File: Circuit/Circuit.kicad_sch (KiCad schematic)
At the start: 2 parts, among them Q1 Q_NMOS_DGS, U1 A1302KUA-T

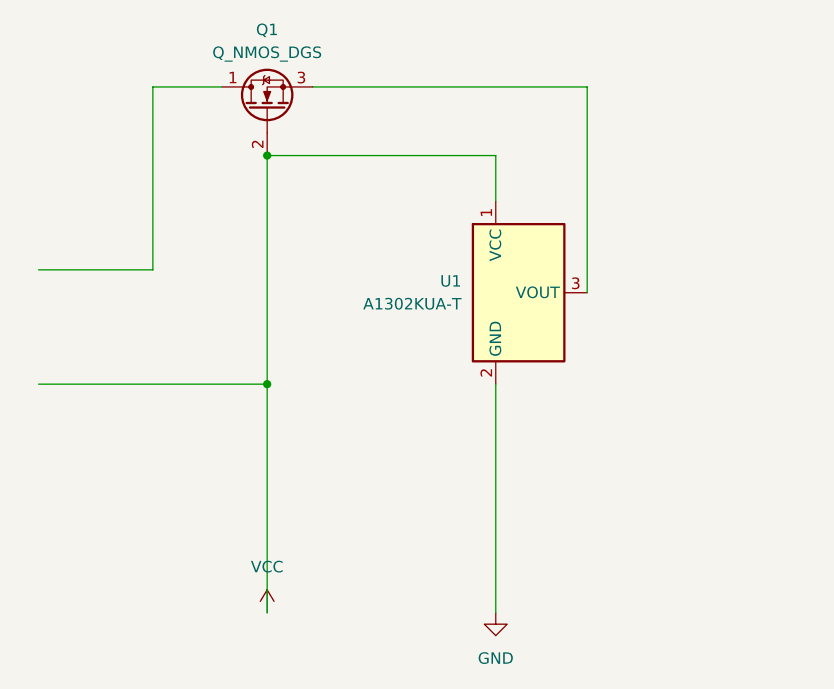
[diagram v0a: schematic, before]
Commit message: Finished circuit, need to test.
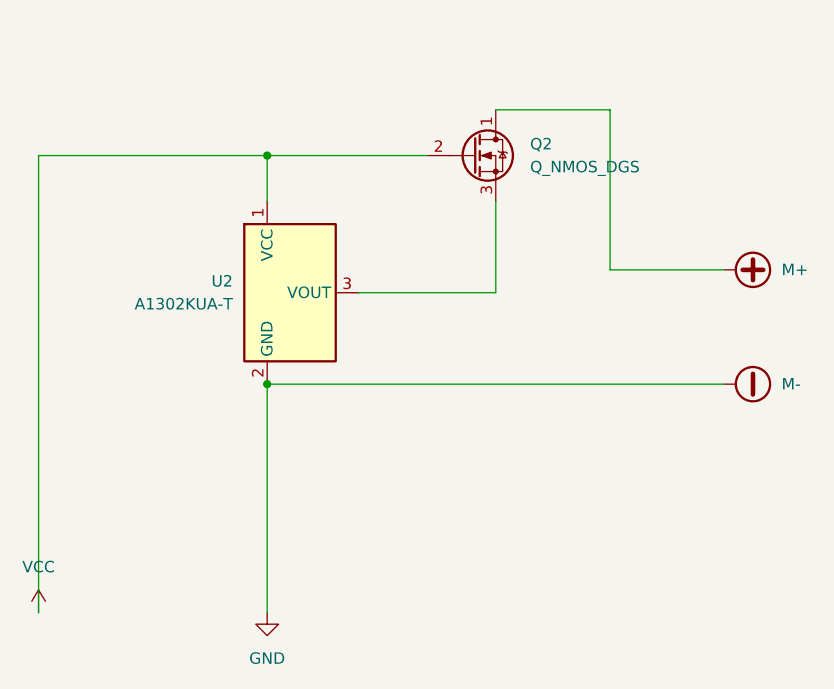
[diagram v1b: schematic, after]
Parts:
- removed Q1: Q_NMOS_DGS, symbol Device:Q_NMOS_DGS
- removed U1: A1302KUA-T, symbol Sensor_Magnetic:A1302KUA-T
- added Q2: Q_NMOS_DGS, symbol Device:Q_NMOS_DGS
- added U2: A1302KUA-T, symbol Sensor_Magnetic:A1302KUA-T
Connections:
- net GND: now also U2.2 (GND)
- net VCC: now also Q2.2 (G), U2.1 (VCC)
- new net: Q2.3 (S), U2.3 (VOUT)
- new net M+: Q2.1 (D)

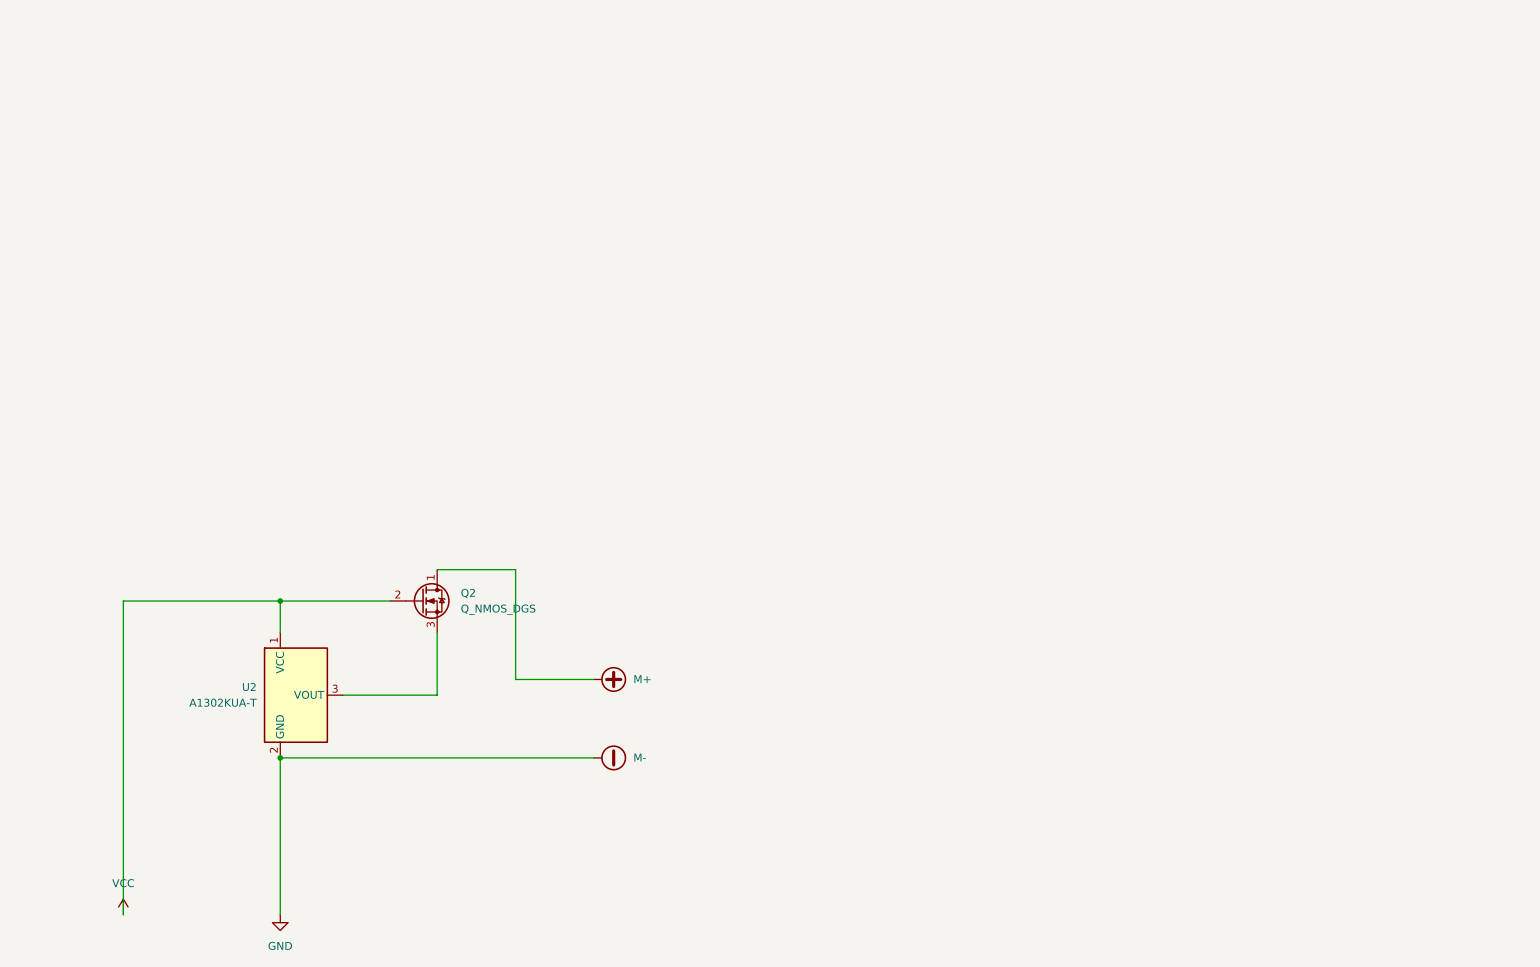
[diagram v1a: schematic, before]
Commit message: Added support for 3 electromagnets and 3 hall chips.
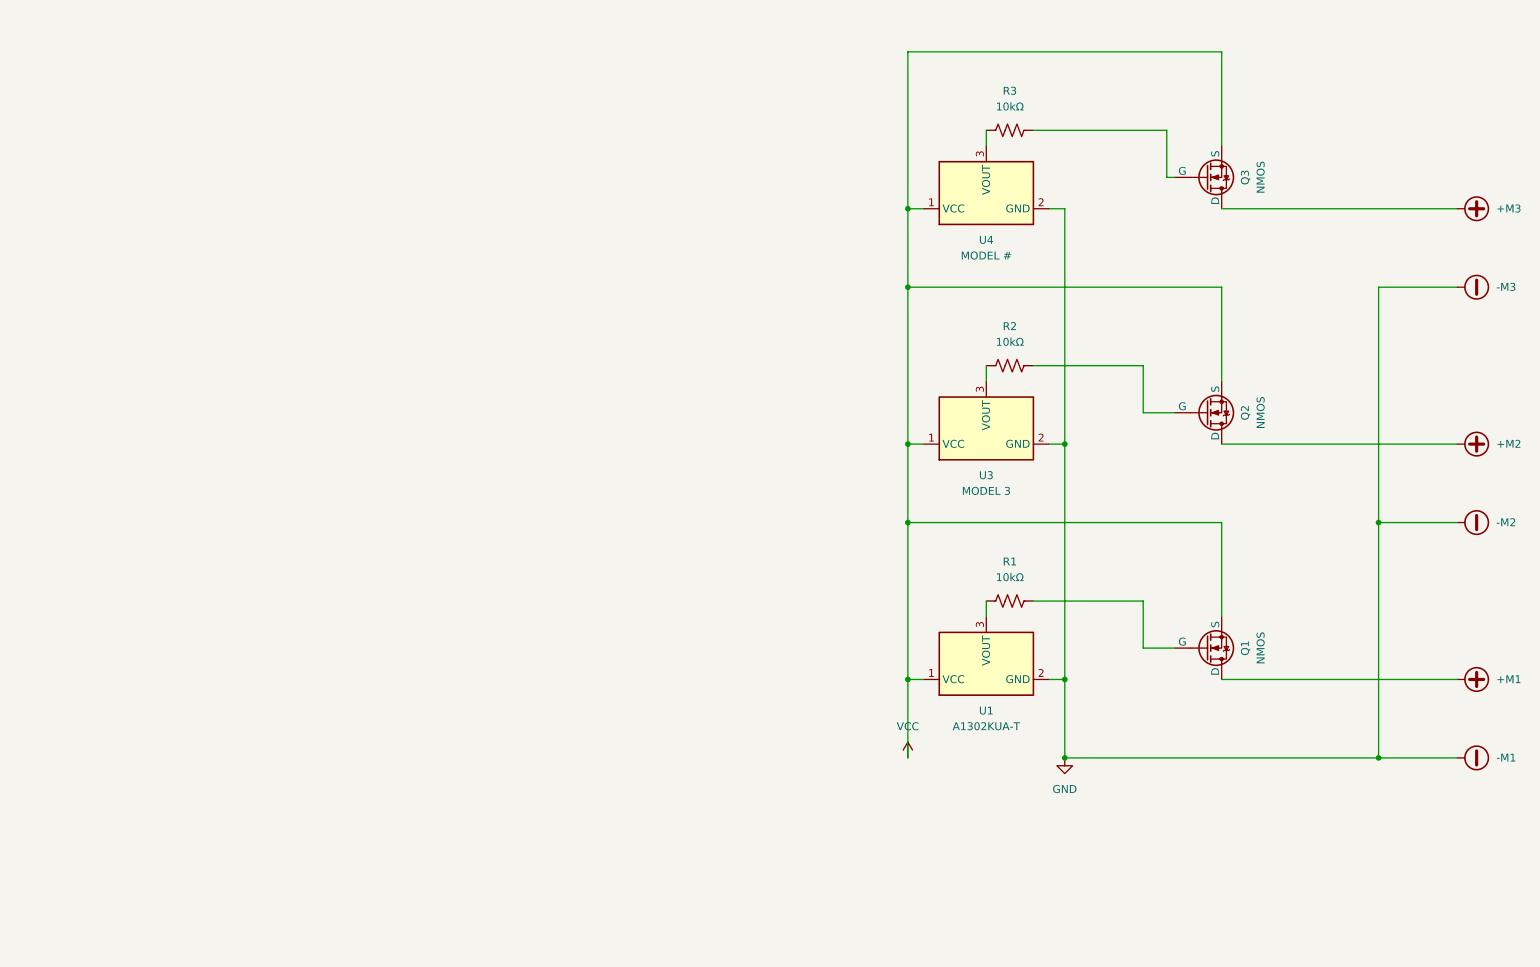
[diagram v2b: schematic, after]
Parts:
- removed Q2: Q_NMOS_DGS, symbol Device:Q_NMOS_DGS
- removed U2: A1302KUA-T, symbol Sensor_Magnetic:A1302KUA-T
- added Q1, Q2, Q3: NMOS, symbol Simulation_SPICE:NMOS
- added R1, R2, R3: 10kΩ, symbol Device:R_US
- added U1: A1302KUA-T, symbol Sensor_Magnetic:A1302KUA-T
- added U3: MODEL 3, symbol Sensor_Magnetic:A1302KUA-T
- added U4: MODEL #, symbol Sensor_Magnetic:A1302KUA-T
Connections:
- net VCC: now also Q1.3 (S), Q2.3 (S), Q3.3 (S), U1.1 (VCC), U3.1 (VCC), U4.1 (VCC)
- new net: Q1.2 (G), R1.2
- new net: R3.1, U4.3 (VOUT)
- new net: Q3.2 (G), R3.2
- new net: Q2.2 (G), R2.2
- new net: R2.1, U3.3 (VOUT)
- new net: R1.1, U1.3 (VOUT)
- new net +M1: Q1.1 (D)
- new net +M2: Q2.1 (D)
- new net +M3: Q3.1 (D)
- new net -M1: U1.2 (GND), U3.2 (GND), U4.2 (GND)

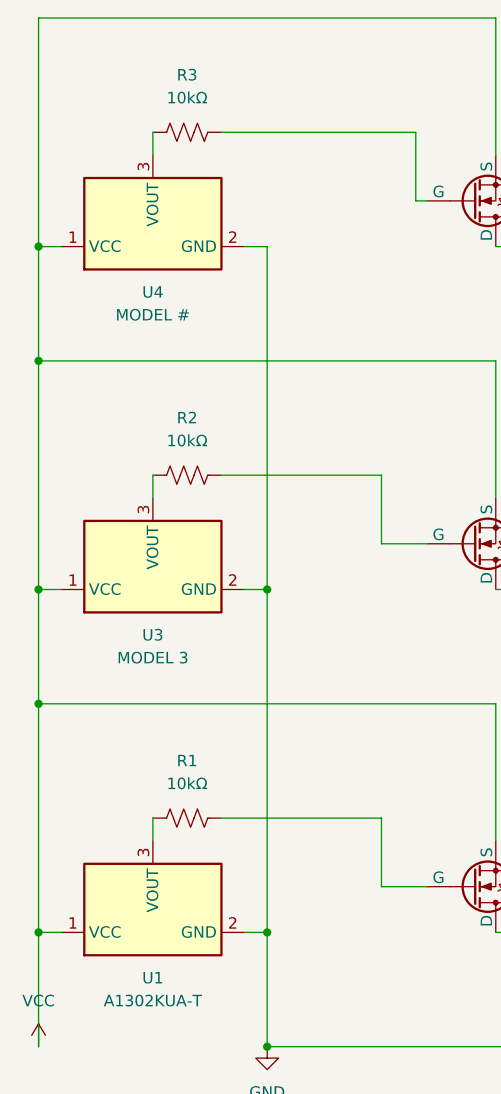
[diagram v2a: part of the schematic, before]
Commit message: Fixed resistors
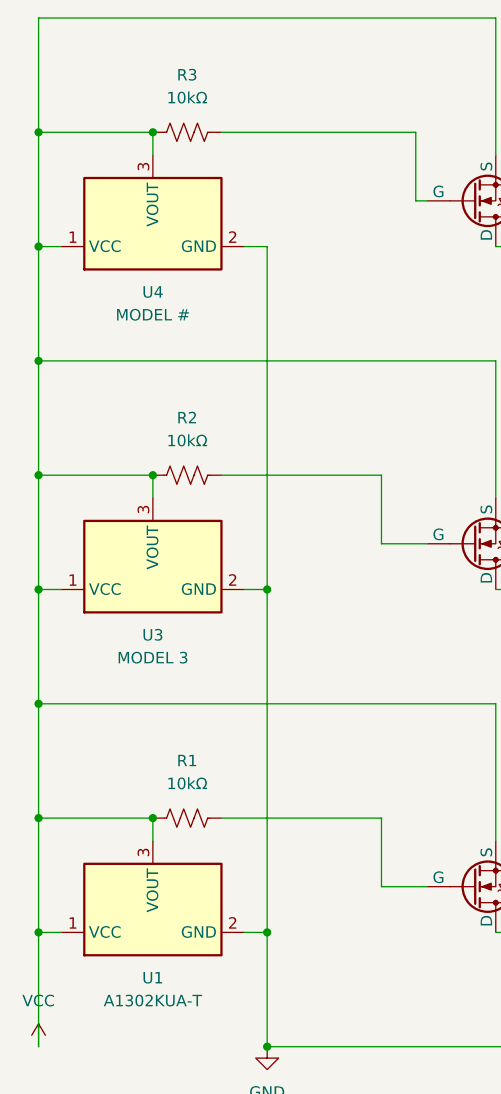
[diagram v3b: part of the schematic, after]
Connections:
- net VCC: now also R1.1, R2.1, R3.1, U1.3 (VOUT), U3.3 (VOUT), U4.3 (VOUT)
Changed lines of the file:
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@@
+	)
+	(junction
+		(at 177.8 139.7)
+		(diameter 0)
+		(color 0 0 0 0)
 	)
 	(junction
@@
 	)
 	(junction
+		(at 165.1 63.5)
+		(diameter 0)
+		(color 0 0 0 0)
+	)
+	(junction
 		(at 241.3 165.1)
 		(diameter 0)
@@
 	)
 	(junction
+		(at 177.8 101.6)
+		(diameter 0)
+		(color 0 0 0 0)
+	)
+	(junction
+		(at 165.1 101.6)
+		(diameter 0)
+		(color 0 0 0 0)
+	)
+	(junction
+		(at 165.1 139.7)
+		(diameter 0)
+		(color 0 0 0 0)
+	)
+	(junction
+		(at 177.8 63.5)
+		(diameter 0)
+		(color 0 0 0 0)
+	)
+	(junction
 		(at 165.1 76.2)
 		(diameter 0)
@@
 	(wire
 		(pts
+			(xy 165.1 139.7) (xy 165.1 127)
+		)
+		(stroke
+			(width 0)
+			(type default)
+		)
+	)
+	(wire
+		(pts
 			(xy 187.96 114.3) (xy 190.5 114.3)
 		)
@@
 	(wire
 		(pts
+			(xy 165.1 139.7) (xy 177.8 139.7)
+		)
+		(stroke
+			(width 0)
+			(type default)
+		)
+	)
+	(wire
+		(pts
 			(xy 215.9 152.4) (xy 254 152.4)
 		)
@@
 	(wire
 		(pts
-			(xy 165.1 152.4) (xy 165.1 127)
+			(xy 165.1 152.4) (xy 165.1 139.7)
 		)
 		(stroke
@@
 	(wire
 		(pts
+			(xy 165.1 63.5) (xy 165.1 76.2)
+		)
+		(stroke
+			(width 0)
+			(type default)
+		)
+	)
+	(wire
+		(pts
 			(xy 215.9 76.2) (xy 254 76.2)
 		)
@@
 	(wire
 		(pts
+			(xy 165.1 63.5) (xy 177.8 63.5)
+		)
+		(stroke
+			(width 0)
+			(type default)
+		)
+	)
+	(wire
+		(pts
 			(xy 190.5 114.3) (xy 190.5 152.4)
 		)
@@
 	(wire
 		(pts
-			(xy 165.1 114.3) (xy 165.1 88.9)
+			(xy 165.1 114.3) (xy 165.1 101.6)
 		)
 		(stroke
@@
 	(wire
 		(pts
-			(xy 165.1 50.8) (xy 165.1 76.2)
-		)
-		(stroke
+			(xy 165.1 50.8) (xy 165.1 63.5)
+		)
+		(stroke
+			(width 0)
+			(type default)
+		)
+	)
+	(wire
+		(pts
+			(xy 165.1 101.6) (xy 177.8 101.6)
+		)
+		(stroke
+			(width 0)
+			(type default)
+		)
+	)
+	(wire
+		(pts
+			(xy 165.1 101.6) (xy 165.1 88.9)
+		)
+		(stroke

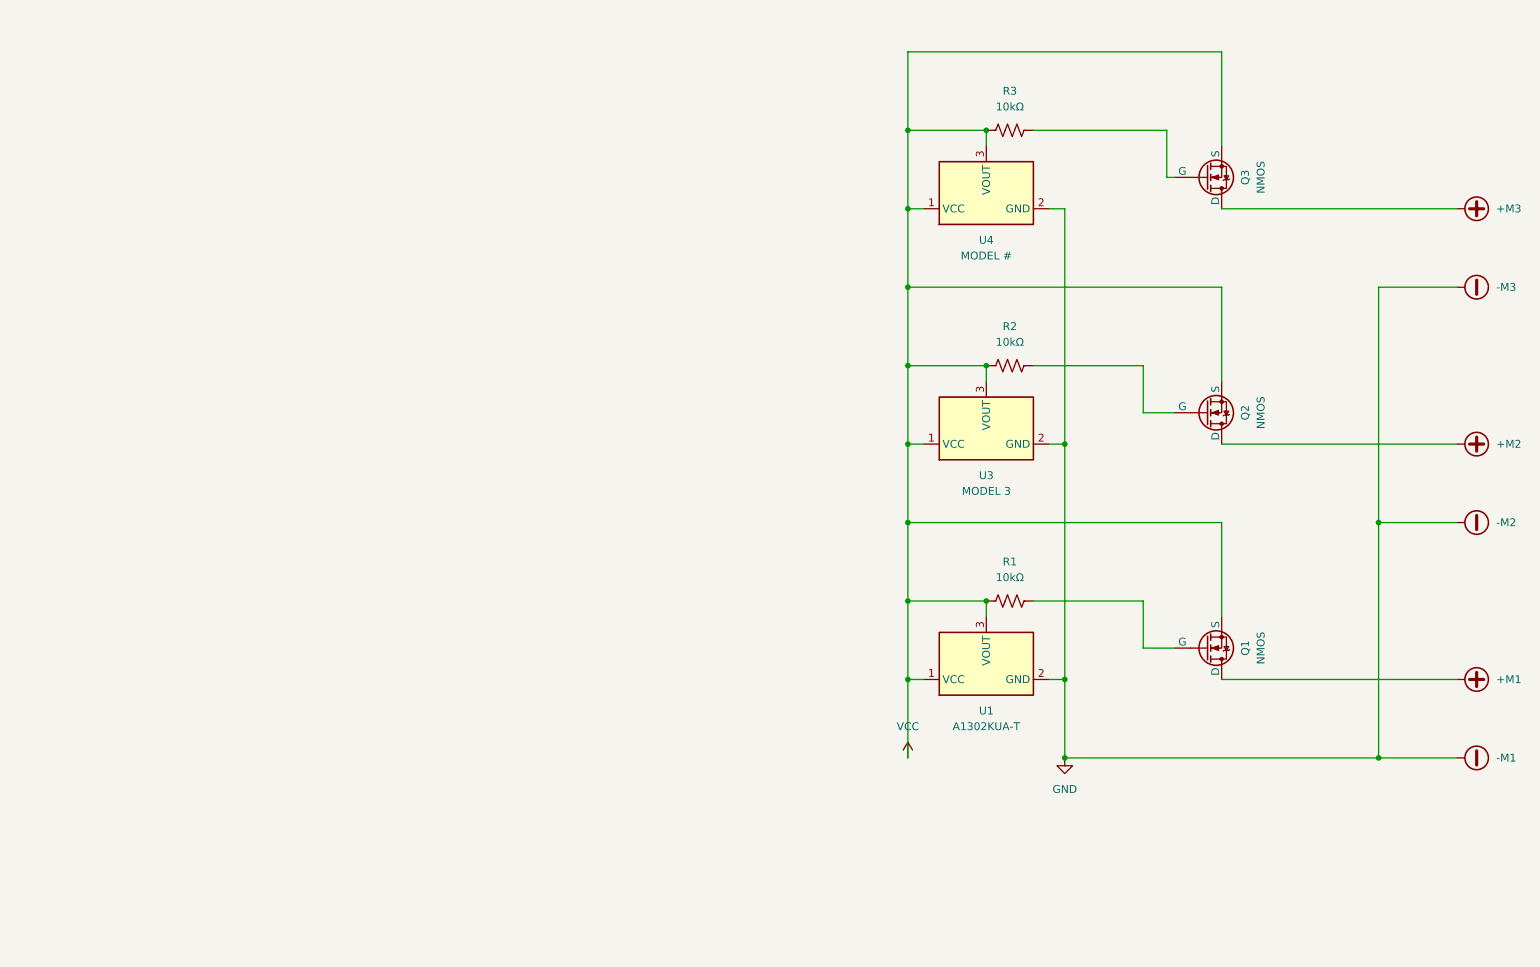
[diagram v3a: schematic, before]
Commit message: Updated circuit to use H-bridge, doesn't work :(
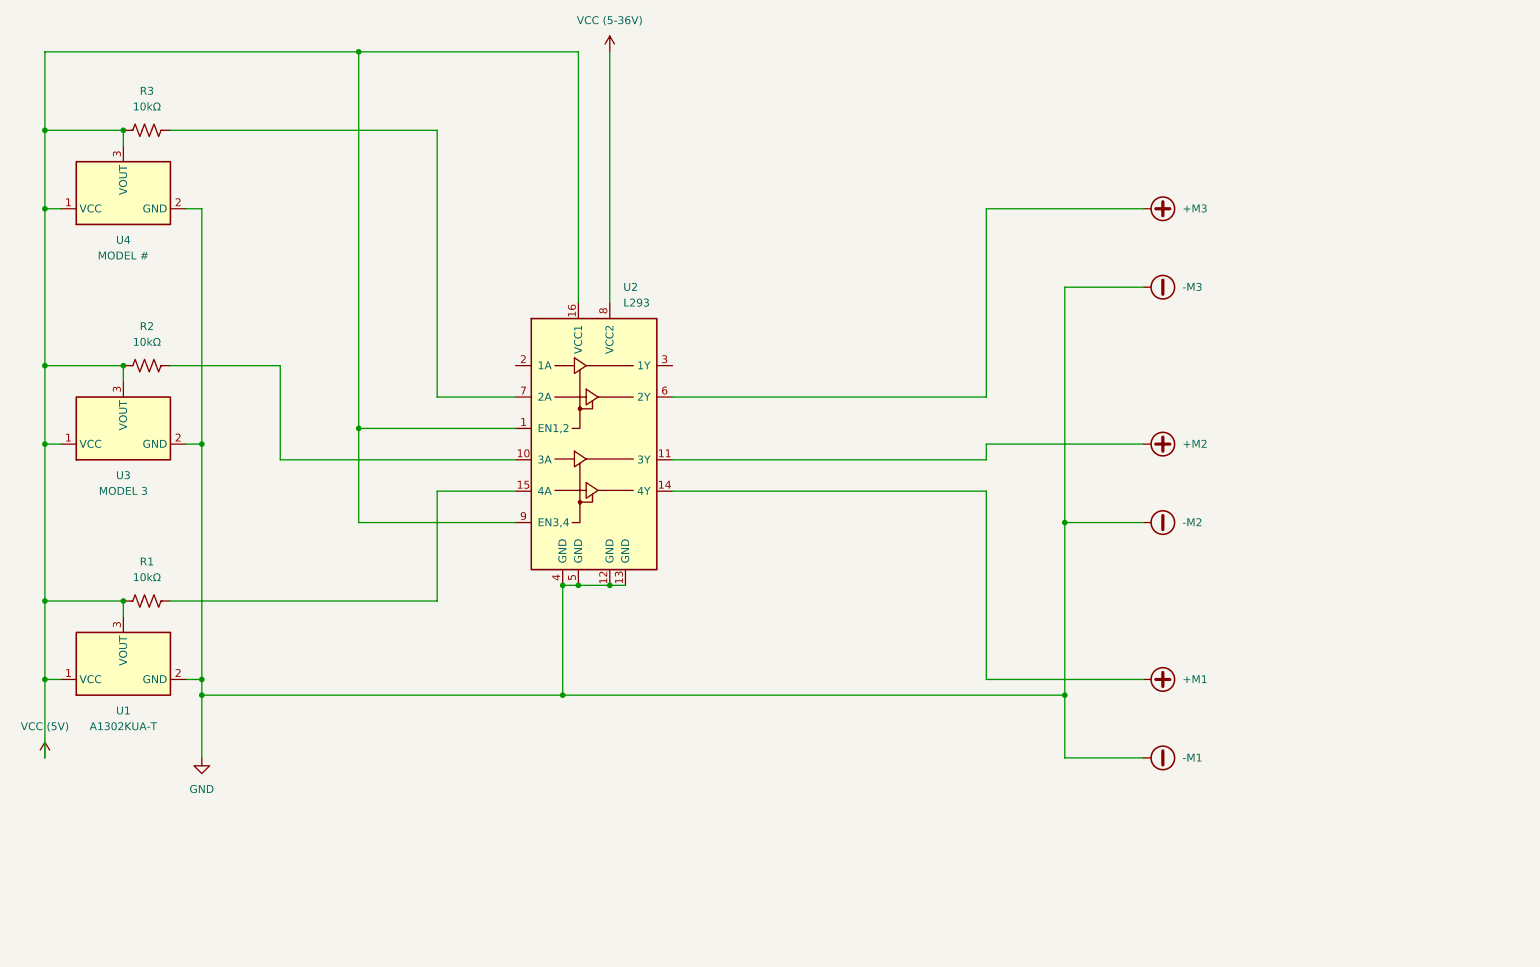
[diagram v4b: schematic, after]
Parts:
- removed Q1, Q2, Q3: NMOS, symbol Simulation_SPICE:NMOS
- added U2: L293, Package_DIP:DIP-16_W7.62mm, symbol Driver_Motor:L293
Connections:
- net +M1: now also U2.14 (4Y)
- net +M2: now also U2.11 (3Y)
- net +M3: now also U2.6 (2Y)
- net -M1: now also U2.12 (GND), U2.13 (GND), U2.4 (GND), U2.5 (GND)
- net at R1.2: now also U2.15 (4A)
- net at R3.2: now also U2.7 (2A)
- net at R2.2: now also U2.10 (3A)
- net VCC renamed VCC (5V)
- net VCC (5V): now also U2.1 (EN1,2), U2.16 (VCC1), U2.9 (EN3,4)
- new net VCC (5-36V): U2.8 (VCC2)
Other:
- moved on the sheet: R1, R2, R3, U1, U3, U4
